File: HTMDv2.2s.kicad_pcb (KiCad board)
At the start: 2 copper layers, 90 x 49.9 mm, 120 parts, among them IC1 TJA1441AT_0Z, IC2 A3921KLPTR-T, IC3 TMP275AQDGKRQ1, J1 Conn_01x04, J10 Conn_01x02, J11 Conn_01x02, J2 Conn_01x04, J3 Conn_01x06, J4 Conn_01x01, J5 Conn_01x01_Pin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

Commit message: update
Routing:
- net +3.3V: track 235.1 -> 232.0 mm
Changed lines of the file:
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@@
   (segment (start 129.7262 74.1172) (end 128.6267 74.1172) (width 0.25) (layer "F.Cu") (net 4))
   (segment (start 138.8364 70.1051) (end 137.8485 69.1172) (width 0.25) (layer "F.Cu") (net 4))
+  (segment (start 140.208 61.4172) (end 141.2748 61.4172) (width 0.8) (layer "F.Cu") (net 4))
   (segment (start 134.649065 54.841165) (end 135.24647 54.841165) (width 0.25) (layer "F.Cu") (net 4))
   (segment (start 148.01127 78.4352) (end 148.87487 77.5716) (width 0.25) (layer "F.Cu") (net 4))
@@
   (segment (start 148.844 77.60247) (end 148.87487 77.5716) (width 0.3) (layer "F.Cu") (net 4))
   (segment (start 128.4213 75.6412) (end 127.762 74.9819) (width 0.25) (layer "F.Cu") (net 4))
-  (segment (start 141.8844 58.6232) (end 141.8844 59.7408) (width 0.3) (layer "F.Cu") (net 4))
   (segment (start 146.6596 78.4352) (end 148.01127 78.4352) (width 0.25) (layer "F.Cu") (net 4))
   (segment (start 129.0817 74.9819) (end 129.1336 74.93) (width 0.25) (layer "F.Cu") (net 4))
@@
   (segment (start 130.0988 66.4972) (end 130.9137 67.3121) (width 0.25) (layer "F.Cu") (net 4))
   (segment (start 130.6892 65.271267) (end 130.0988 65.861667) (width 0.25) (layer "F.Cu") (net 4))
-  (segment (start 141.8844 59.7408) (end 140.208 61.4172) (width 0.3) (layer "F.Cu") (net 4))
+  (segment (start 141.8844 60.8076) (end 141.8844 58.6232) (width 0.8) (layer "F.Cu") (net 4))
   (segment (start 139.675286 70.282214) (end 141.599607 70.282214) (width 0.25) (layer "F.Cu") (net 4))
   (segment (start 135.2587 64.356) (end 136.3179 63.2968) (width 0.25) (layer "F.Cu") (net 4))
@@
   (segment (start 133.6863 55.1362) (end 134.3152 54.5073) (width 0.25) (layer "F.Cu") (net 4))
   (segment (start 125.0547 83.1998) (end 124.9547 83.2998) (width 0.25) (layer "F.Cu") (net 4))
+  (segment (start 141.2748 61.4172) (end 141.8844 60.8076) (width 0.8) (layer "F.Cu") (net 4))
   (segment (start 129.2352 87.63) (end 130.2531 87.63) (width 0.3) (layer "F.Cu") (net 4))
   (segment (start 118.131101 78.363299) (end 116.313103 78.363299) (width 0.25) (layer "F.Cu") (net 4))
@@
   (via (at 125.0547 81.026) (size 0.6) (drill 0.3) (layers "F.Cu" "B.Cu") (net 4))
   (segment (start 122.2248 78.3844) (end 118.152202 78.3844) (width 0.25) (layer "B.Cu") (net 4))
-  (segment (start 148.87487 77.5716) (end 148.87487 69.7992) (width 0.3) (layer "B.Cu") (net 4))
-  (segment (start 144.9324 55.960901) (end 142.870299 55.960901) (width 0.3) (layer "B.Cu") (net 4))
+  (segment (start 148.87487 56.87607) (end 148.87487 69.9516) (width 0.4) (layer "B.Cu") (net 4))
   (segment (start 136.1326 57.1894) (end 136.0932 57.2288) (width 0.25) (layer "B.Cu") (net 4))
-  (segment (start 114.3508 86.4672) (end 112.247975 86.4672) (width 0.25) (layer "B.Cu") (net 4))
   (segment (start 125.0188 86.6648) (end 125.3772 87.0232) (width 0.25) (layer "B.Cu") (net 4))
-  (segment (start 106.949716 86.9696) (end 107.452116 86.4672) (width 0.3) (layer "B.Cu") (net 4))
-  (segment (start 148.87487 69.7992) (end 148.87487 56.82527) (width 0.3) (layer "B.Cu") (net 4))
+  (segment (start 147.909701 55.910901) (end 148.87487 56.87607) (width 0.4) (layer "B.Cu") (net 4))
+  (segment (start 106.949716 86.9696) (end 85.562917 86.9696) (width 0.3) (layer "B.Cu") (net 4))
+  (segment (start 113.3348 86.4672) (end 112.247975 86.4672) (width 0.25) (layer "B.Cu") (net 4))
   (segment (start 125.3772 87.0232) (end 127.1044 87.0232) (width 0.25) (layer "B.Cu") (net 4))
+  (segment (start 143.9716 57.21) (end 144.0088 57.21) (width 0.8) (layer "B.Cu") (net 4))
   (segment (start 135.24647 53.860184) (end 135.24647 53.76327) (width 0.25) (layer "B.Cu") (net 4))
+  (segment (start 115.411394 88.4428) (end 125.6848 88.4428) (width 0.3) (layer "B.Cu") (net 4))
+  (segment (start 85.562917 86.9696) (end 85.5472 86.953883) (width 0.3) (layer "B.Cu") (net 4))
+  (segment (start 113.3348 86.4672) (end 113.435794 86.4672) (width 0.3) (layer "B.Cu") (net 4))
+  (segment (start 107.452116 86.4672) (end 106.949716 86.9696) (width 0.3) (layer "B.Cu") (net 4))
+  (segment (start 125.6848 88.4428) (end 127.1044 87.0232) (width 0.3) (layer "B.Cu") (net 4))
   (segment (start 147.96047 70.7136) (end 148.87487 69.7992) (width 0.25) (layer "B.Cu") (net 4))
-  (segment (start 114.3508 86.4672) (end 114.3508 87.382206) (width 0.3) (layer "B.Cu") (net 4))
   (segment (start 131.5722 50.089) (end 117.612 50.089) (width 0.25) (layer "B.Cu") (net 4))
   (segment (start 148.844 80.9752) (end 143.352 86.4672) (width 0.3) (layer "B.Cu") (net 4))
   (segment (start 129.1844 87.6808) (end 127.9708 86.4672) (width 0.3) (layer "B.Cu") (net 4))
   (segment (start 130.6892 65.271267) (end 130.695933 65.278) (width 0.25) (layer "B.Cu") (net 4))
-  (segment (start 148.010501 55.960901) (end 144.9324 55.960901) (width 0.3) (layer "B.Cu") (net 4))
+  (segment (start 144.0088 57.21) (end 145.307899 55.910901) (width 0.4) (layer "B.Cu") (net 4))
+  (segment (start 112.247975 86.4672) (end 111.755368 86.959807) (width 0.25) (layer "B.Cu") (net 4))
   (segment (start 129.1336 74.93) (end 125.0547 79.0089) (width 0.25) (layer "B.Cu") (net 4))
   (segment (start 109.255 47.464) (end 107.93 48.789) (width 0.25) (layer "B.Cu") (net 4))
   (segment (start 125.0547 79.0089) (end 125.0547 81.026) (width 0.25) (layer "B.Cu") (net 4))
   (segment (start 143.352 86.4672) (end 127.6604 86.4672) (width 0.3) (layer "B.Cu") (net 4))
-  (segment (start 141.8844 56.9468) (end 141.8844 58.6232) (width 0.3) (layer "B.Cu") (net 4))
+  (segment (start 148.87487 69.9516) (end 148.87487 69.7992) (width 0.3) (layer "B.Cu") (net 4))
   (segment (start 114.987 47.464) (end 109.255 47.464) (width 0.25) (layer "B.Cu") (net 4))
-  (segment (start 148.87487 56.82527) (end 148.010501 55.960901) (width 0.3) (layer "B.Cu") (net 4))
-  (segment (start 125.6848 88.4428) (end 127.1044 87.0232) (width 0.3) (layer "B.Cu") (net 4))
-  (segment (start 107.452116 86.4672) (end 114.3508 86.4672) (width 0.3) (layer "B.Cu") (net 4))
   (segment (start 136.0932 60.620783) (end 136.121603 60.649186) (width 0.25) (layer "B.Cu") (net 4))
   (segment (start 142.030993 70.7136) (end 147.96047 70.7136) (width 0.25) (layer "B.Cu") (net 4))
   (segment (start 135.24647 53.76327) (end 131.5722 50.089) (width 0.25) (layer "B.Cu") (net 4))
+  (segment (start 148.87487 77.5716) (end 148.87487 69.9516) (width 0.3) (layer "B.Cu") (net 4))
   (segment (start 127.217799 86.909801) (end 127.6604 86.4672) (width 0.25) (layer "B.Cu") (net 4))
   (segment (start 143.9716 57.21) (end 143.9716 56.921701) (width 0.25) (layer "B.Cu") (net 4))
   (segment (start 130.695933 65.278) (end 133.4008 65.278) (width 0.25) (layer "B.Cu") (net 4))
-  (segment (start 142.870299 55.960901) (end 141.8844 56.9468) (width 0.3) (layer "B.Cu") (net 4))
+  (segment (start 145.307899 55.910901) (end 147.909701 55.910901) (width 0.4) (layer "B.Cu") (net 4))
   (segment (start 127.1044 87.0232) (end 127.6604 86.4672) (width 0.3) (layer "B.Cu") (net 4))
-  (segment (start 143.9716 56.921701) (end 144.9324 55.960901) (width 0.25) (layer "B.Cu") (net 4))
+  (segment (start 113.3348 86.4672) (end 107.452116 86.4672) (width 0.3) (layer "B.Cu") (net 4))
   (segment (start 136.0932 57.2288) (end 136.0932 60.620783) (width 0.25) (layer "B.Cu") (net 4))
-  (segment (start 85.5472 86.953883) (end 85.562917 86.9696) (width 0.3) (layer "B.Cu") (net 4))
-  (segment (start 85.562917 86.9696) (end 106.949716 86.9696) (width 0.3) (layer "B.Cu") (net 4))
   (segment (start 116.312 48.789) (end 114.987 47.464) (width 0.25) (layer "B.Cu") (net 4))
-  (segment (start 115.411394 88.4428) (end 125.6848 88.4428) (width 0.3) (layer "B.Cu") (net 4))
+  (segment (start 143.9716 57.21) (end 143.2976 57.21) (width 0.8) (layer "B.Cu") (net 4))
+  (segment (start 113.435794 86.4672) (end 115.411394 88.4428) (width 0.3) (layer "B.Cu") (net 4))
   (segment (start 148.844 79.8576) (end 148.844 80.9752) (width 0.3) (layer "B.Cu") (net 4))
   (segment (start 141.983014 70.665621) (end 142.030993 70.7136) (width 0.25) (layer "B.Cu") (net 4))
+  (segment (start 143.2976 57.21) (end 141.8844 58.6232) (width 0.8) (layer "B.Cu") (net 4))
   (segment (start 118.152202 78.3844) (end 118.131101 78.363299) (width 0.25) (layer "B.Cu") (net 4))
-  (segment (start 114.3508 87.382206) (end 115.411394 88.4428) (width 0.3) (layer "B.Cu") (net 4))
   (segment (start 127.9708 86.4672) (end 127.6604 86.4672) (width 0.3) (layer "B.Cu") (net 4))
-  (segment (start 112.247975 86.4672) (end 111.755368 86.959807) (width 0.25) (layer "B.Cu") (net 4))
   (segment (start 117.612 50.089) (end 116.312 48.789) (width 0.25) (layer "B.Cu") (net 4))
   (segment (start 111.070739 64.0043) (end 111.095239 64.0288) (width 0.4) (layer "F.Cu") (net 5))
@@
   (segment (start 91.2025 83.8328) (end 94.6521 83.8328) (width 0.25) (layer "F.Cu") (net 6))
   (segment (start 94.6521 83.8328) (end 95.4521 84.6328) (width 0.25) (layer "F.Cu") (net 6))
+  (segment (start 140.696 48.789) (end 140.696 51.5527) (width 0.6) (layer "F.Cu") (net 6))
   (segment (start 102.6141 86.5124) (end 102.5761 86.4744) (width 0.25) (layer "F.Cu") (net 6))
   (segment (start 144.3228 52.1716) (end 140.0771 52.1716) (width 0.3) (layer "F.Cu") (net 6))
@@
   (segment (start 127.1832 47.0696) (end 127.1832 48.789) (width 0.6) (layer "F.Cu") (net 6))
   (segment (start 135.382 61.4172) (end 134.3152 61.4172) (width 0.25) (layer "F.Cu") (net 6))
-  (segment (start 140.696 51.5527) (end 140.0263 52.2224) (width 0.3) (layer "F.Cu") (net 6))
+  (segment (start 140.696 51.5527) (end 140.0263 52.2224) (width 0.6) (layer "F.Cu") (net 6))
   (segment (start 98.4784 86.4744) (end 98.0948 86.0908) (width 0.25) (layer "F.Cu") (net 6))
-  (segment (start 140.696 48.789) (end 140.696 51.5527) (width 0.3) (layer "F.Cu") (net 6))
   (segment (start 89.9453 85.09) (end 91.2025 83.8328) (width 0.25) (layer "F.Cu") (net 6))
   (segment (start 95.4521 84.6328) (end 95.9104 84.6328) (width 0.25) (layer "F.Cu") (net 6))

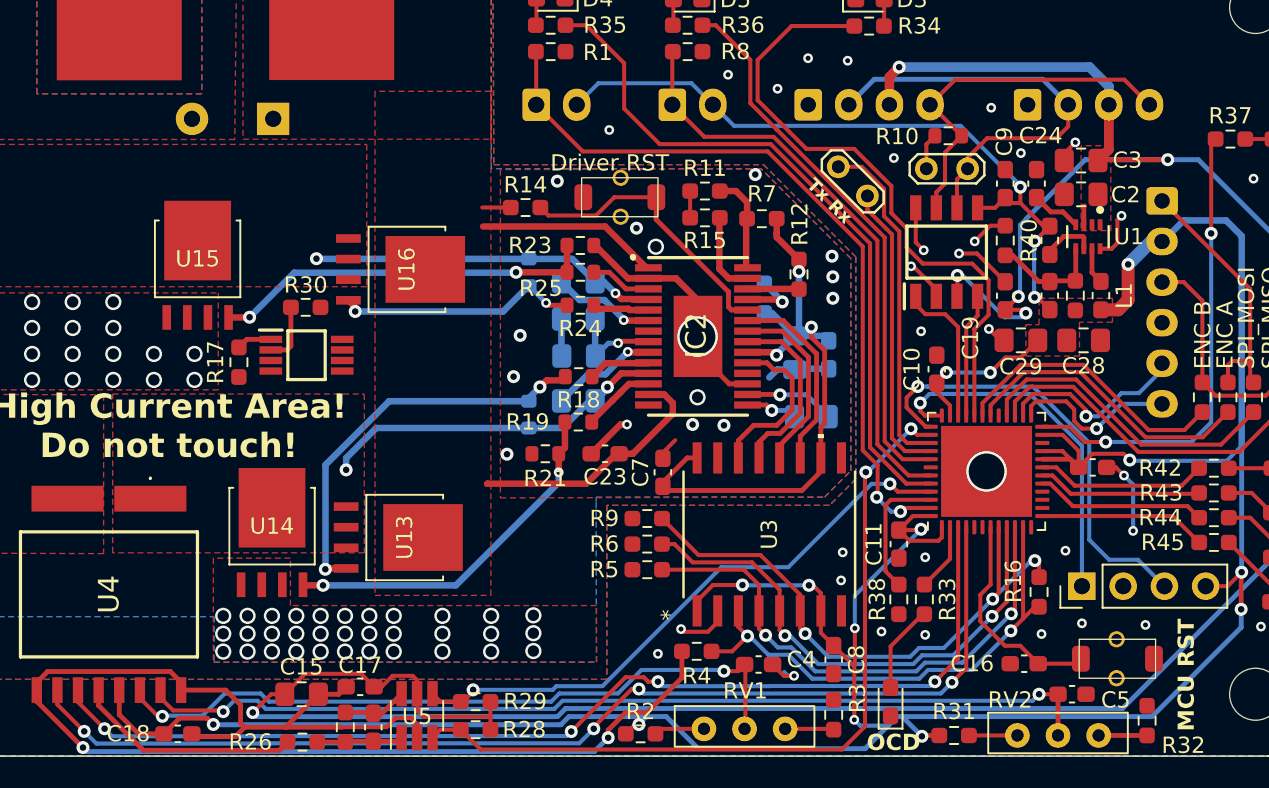
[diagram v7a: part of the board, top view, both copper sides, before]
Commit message: update
change 3D models
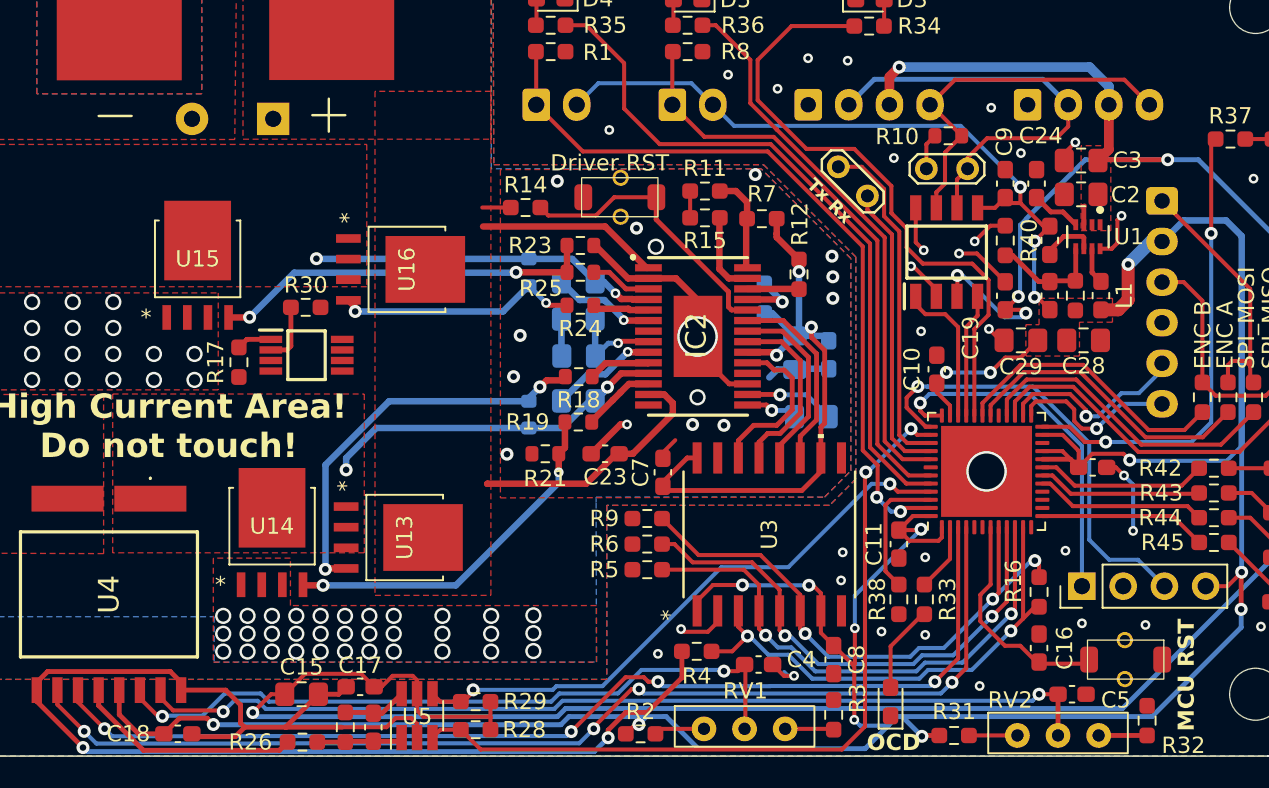
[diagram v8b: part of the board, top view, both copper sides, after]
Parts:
- U13, U14, U15: value SQJ180EP-T1_GE3 -> PowerPAK_SO-8L_3_VIS
- moved C16 1.33 mm to (136.4, 82.2), turned to 90 degrees
- moved SW2 0.51 mm to (141.7, 83.0)
